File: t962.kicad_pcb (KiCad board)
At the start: 2 copper layers, 40 x 45 mm, 40 parts, among them J1 Conn_01x03, J10 Conn_01x04, J2 TE 282834-8, J3 JST XH-B02B-XH-AM, J4 Conn_01x02_Male, J5 JST XH-B02B-XH-AM, J6 JST XH-B02B-XH-AM, J7 2.54mm pin header, J8 USB_B_Micro, J9 Conn_01x03_Male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

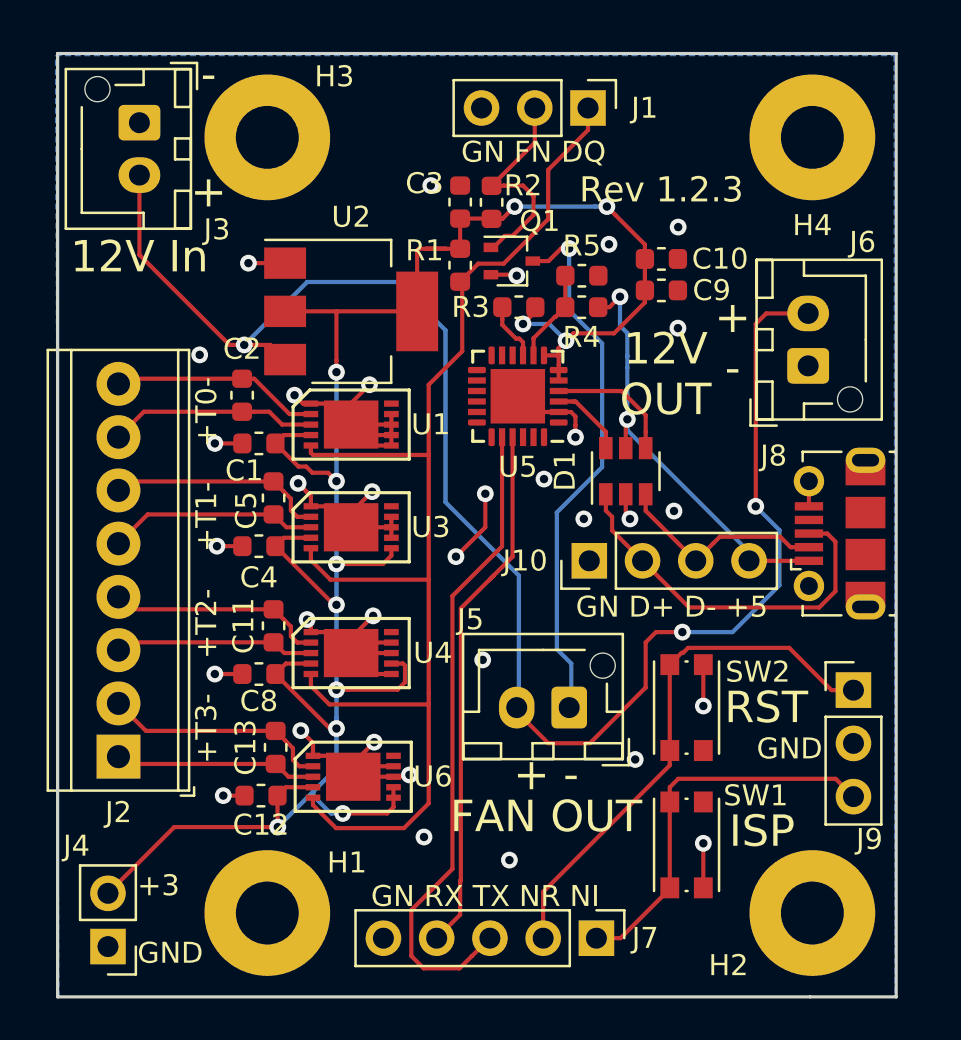
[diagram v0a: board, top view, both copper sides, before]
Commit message: Modified design for USB-C.  This also switches the pins for rx and tx with the UART and changes the CP2102 to a CP2104.  UART indicator LEDs were also added and various issues were cleaned up on the PCB.  Power traces are also fatter.
Signed-off-by: Aaron Williams <aaron.w2@gmail.com>
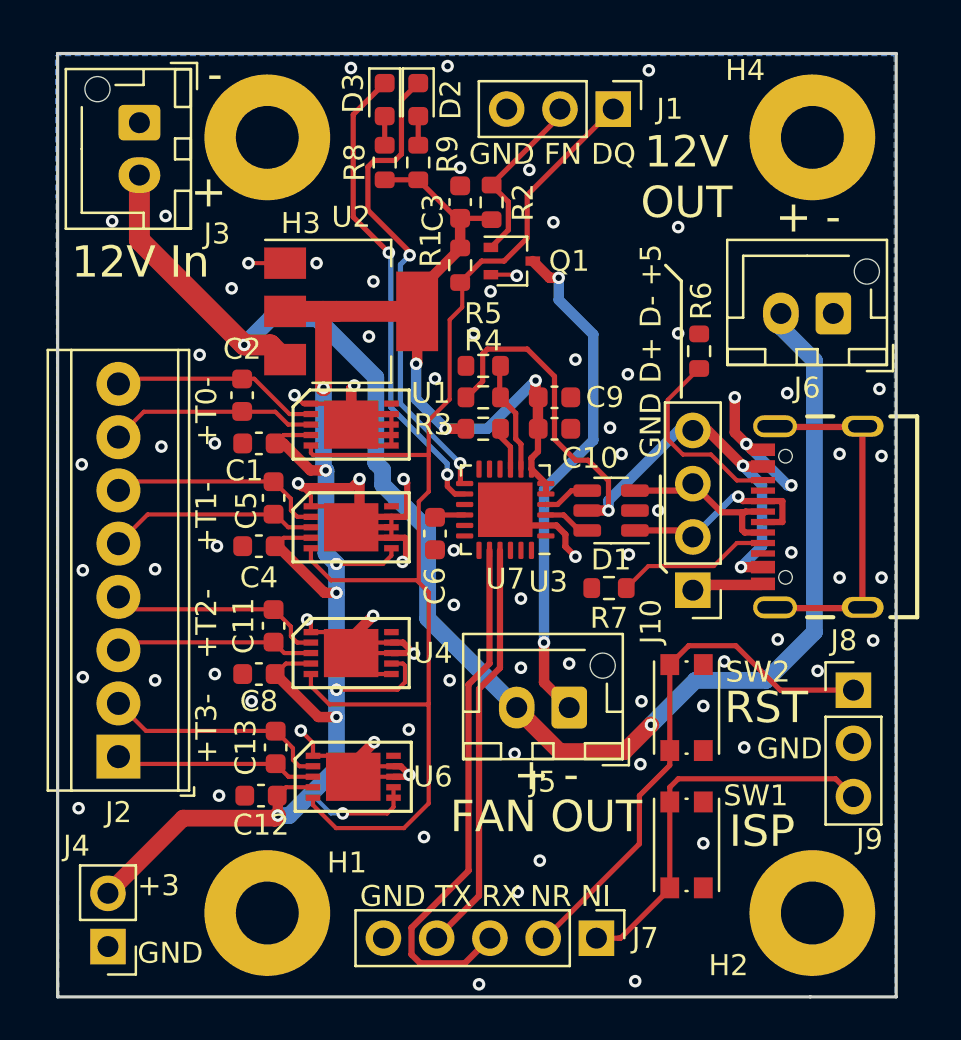
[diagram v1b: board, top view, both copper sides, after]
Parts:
- removed U5: CP2102N-A01-QFN24, Aaron:QFN-24-1EP_4x4mm_Pitch0.5mm_rounded_corners
- added C6: 4.7uF, Capacitor_SMD:C_0603_1608Metric, F.Cu at (145.9, 54.0)
- added D2: Red, LED_SMD:LED_0603_1608Metric, F.Cu at (145.1, 33.3)
- added D3: Green, LED_SMD:LED_0603_1608Metric, F.Cu at (143.5, 33.3)
- added R6: 5.1K, Resistor_SMD:R_0603_1608Metric, F.Cu at (158.5, 45.3)
- added R7: 5.1K, Resistor_SMD:R_0603_1608Metric, F.Cu at (154.2, 56.6)
- added R8: 560, Resistor_SMD:R_0603_1608Metric, F.Cu at (143.5, 36.3)
- added R9: 560, Resistor_SMD:R_0603_1608Metric, F.Cu at (145.1, 36.3)
- added U7: CP2104, Package_DFN_QFN:QFN-24-1EP_4x4mm_P0.5mm_EP2.6x2.6mm, F.Cu at (149.2, 52.9)
- J3, J5, J6: footprint Connector_JST:JST_XH_B02B-XH-AM_1x02_P2.50mm_Vertical -> Connector_JST:JST_XH_B2B-XH-AM_1x02_P2.50mm_Vertical
- J8: value USB_B_Micro -> USB_C_Receptacle_USB2.0; footprint Aaron:USB_Micro-B_Molex-105017-0001 -> Aaron:GCT_USB4105-GF-A
- R4: value 22.1K -> 24K
- moved C10 9.57 mm to (151.6, 49.0)
- moved C9 7.21 mm to (151.6, 47.5)
- moved R5 6.37 mm to (148.2, 46.0), turned to 180 degrees
- moved R4 6.37 mm to (148.2, 47.5), turned to 0 degrees
- moved R3 6.04 mm to (148.2, 49.0), turned to 0 degrees
- moved J10 5.13 mm to (158.2, 56.7), turned to 180 degrees
- moved J6 2.77 mm to (164.9, 43.5), turned to 180 degrees
- moved D1 2.00 mm to (154.3, 52.9), turned to 180 degrees
- moved J8 1.36 mm to (166.3, 53.2)
- moved J1 1.20 mm to (154.4, 33.8)
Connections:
- J7 pad 3: /TXD0 -> /RXD0
- J7 pad 4: /RXD0 -> /TXD0
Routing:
- net /RX_LED: track 0.00 -> 22.9 mm, vias 0 -> 2
- net /TX_LED: track 0.00 -> 22.7 mm, vias 0 -> 2
- net unconnected-(J8-SHIELD-PadS1): track 0.00 -> 17.0 mm
- net /TXD0: track 31.1 -> 19.8 mm
- net +5V: track 20.9 -> 31.9 mm, vias 2 -> 3
- net /CC2: track 0.00 -> 9.34 mm
- net /D+: track 18.1 -> 9.53 mm, vias 0 -> 1
- net /CC1: track 0.00 -> 7.41 mm
- net GND: track 70.8 -> 65.9 mm, vias 33 -> 83
- net /P_D-: track 6.20 -> 2.25 mm
- net /FAN_PWM: track 10.4 -> 8.26 mm
- net /D-: track 10.2 -> 8.24 mm
- net +12V: track 77.5 -> 75.6 mm, vias 3 -> 2
- net /P_D+: track 3.63 -> 1.90 mm
- net +3V3: track 106.9 -> 105.4 mm, vias 12 -> 11
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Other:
- net class Default removed
- rule pad_to_mask_clearance: 0.0504 -> 0.0508
- board text added: "GND D+ D- +5"
- board text added: "GND FN DQ"
- board text added: "GND TX RX NR NI"
- board text added: "Rev ${REVISION}"
- board text removed: "GN D+ D- +5"
- board text removed: "GN FN DQ"
- board text removed: "GN RX TX NR NI"
- board text removed: "Rev 1.2.3"
